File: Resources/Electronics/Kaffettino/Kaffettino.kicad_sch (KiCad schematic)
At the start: 6 parts, among them SW1 SW_Push, SW2 SW_Push, SW3 SW_Push

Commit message: PCB Design - continuing schema
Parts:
- removed SW1, SW2, SW3: SW_Push, symbol Switch:SW_Push
- added Brd1: SSD1306, Display:Adafruit_SSD1306, symbol SSD1306-128x64_OLED:SSD1306
- added C1, C2, C3: 100nF, symbol Device:C
- added J1: 1984659, CONN_1984659_PXC, symbol 2025-11-03_20-57-13:1984659
- added M1: RFID-RC522, RFID-RC522:RFID-RC522, symbol RFID-RC522:RFID-RC522
- added R1, R2, R3: 330, symbol Device:R
- added R4, R5, R6: 1k, symbol Device:R
- added R7, R8, R9: 10k, symbol Device:R
- D1: value LED -> Green
- D2: value LED -> Yellow
- D3: value LED -> Red
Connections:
- net at D3.1 (K): now also R3.1
- net at D2.1 (K): now also R2.1
- net at D1.1 (K): now also R1.1
- new net: C1.1, R4.1, R7.2
- new net: J1.4, R4.2
- new net: C2.1, R6.1, R9.2
- new net: C3.1, R5.1, R8.2
- new net: J1.5, R6.2
- new net: J1.6, R5.2
- new net +3.3V: R7.1, R8.1, R9.1
- new net GNDREF: Brd1.1 (GND), C1.2, C2.2, C3.2, J1.1, J1.2, J1.3, M1.6 (GND), R1.2, R2.2, R3.2
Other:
- company: (none) -> Vivere Ingegneria
- title: (none) -> Scheda superiore kaffettino
- moved on the sheet: D1, D2, D3

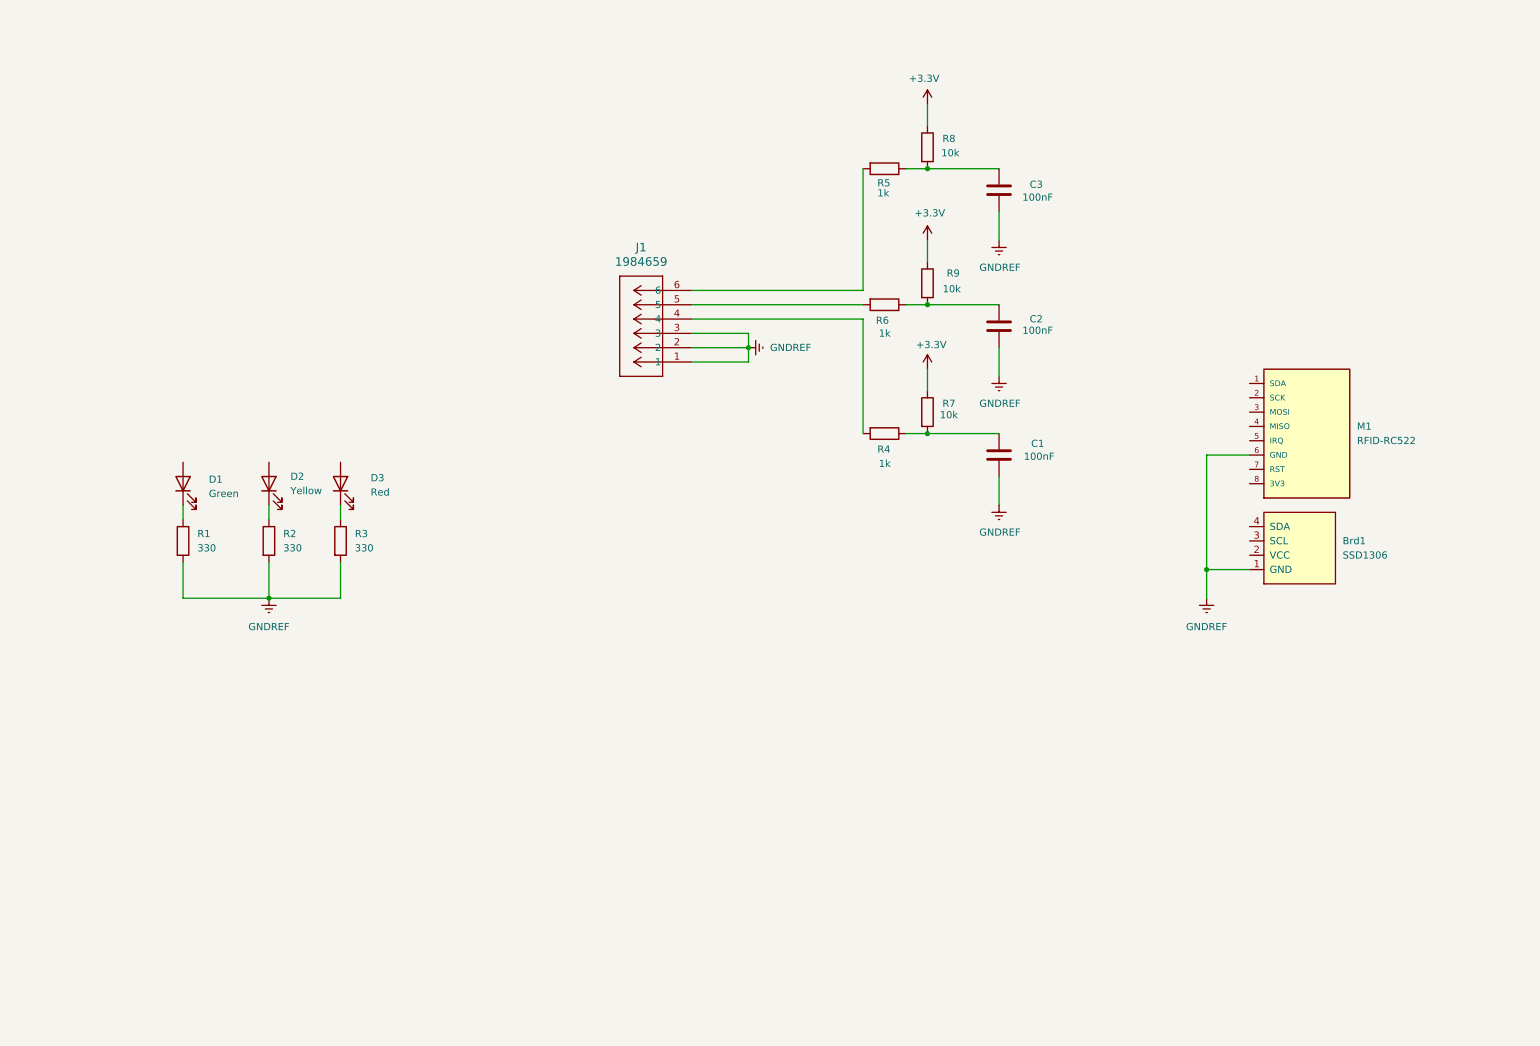
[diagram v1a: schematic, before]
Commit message: Finished electrical schema and removed node_modules
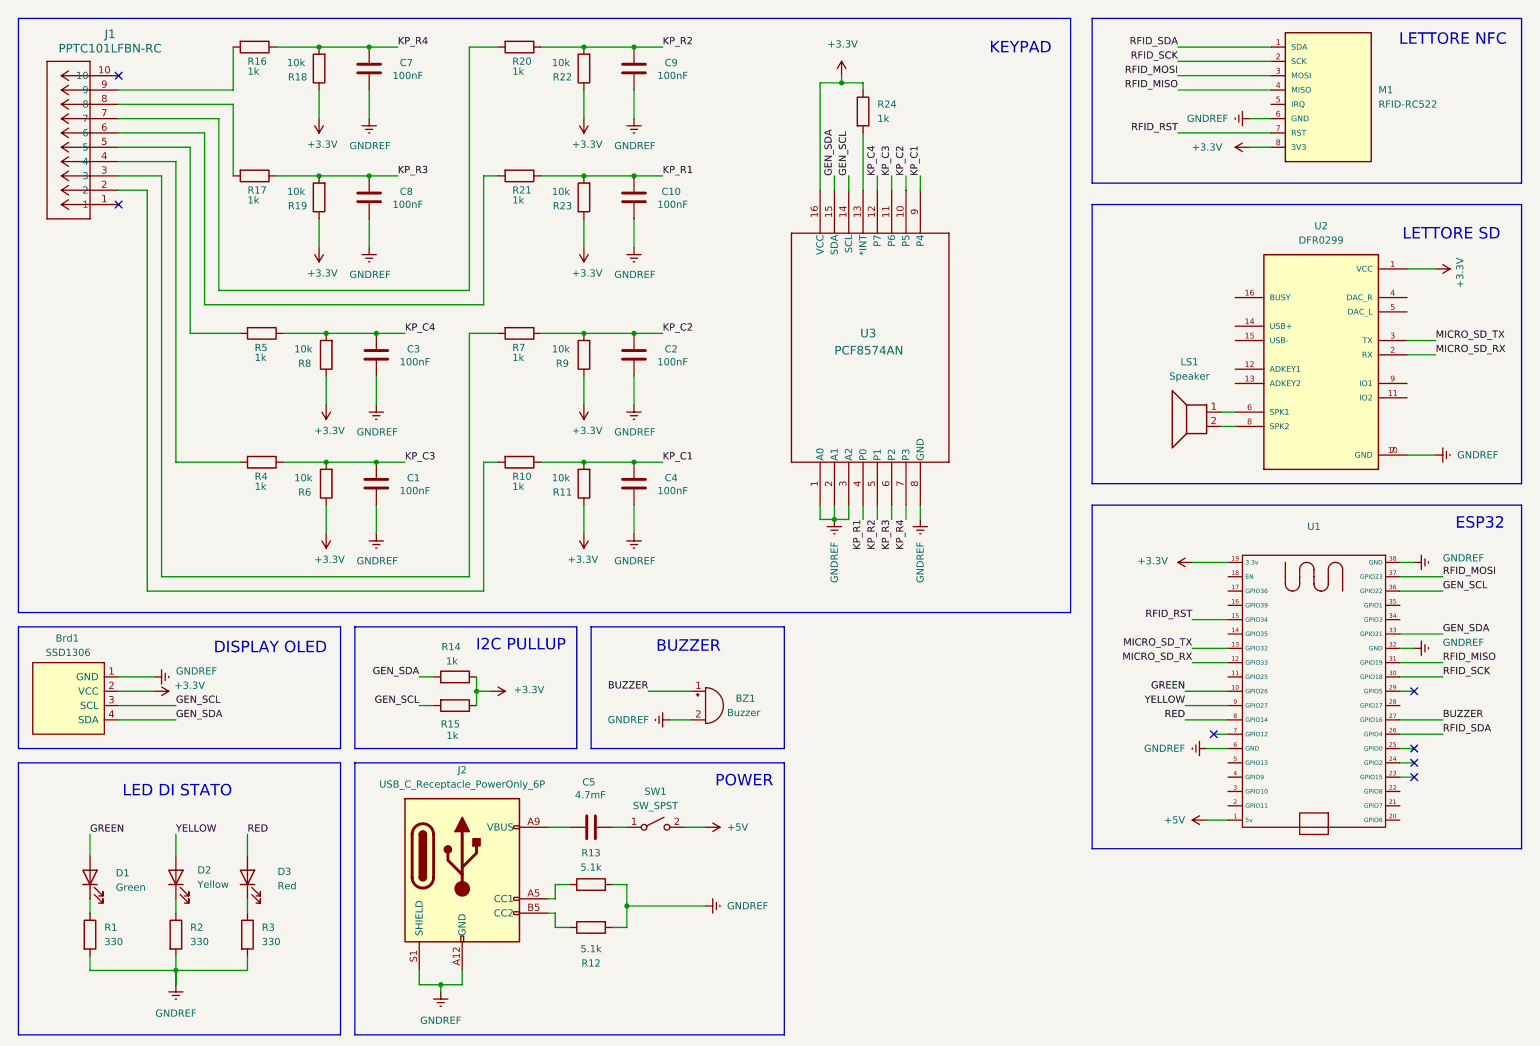
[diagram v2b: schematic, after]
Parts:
- removed J1: 1984659, CONN_1984659_PXC, symbol 2025-11-03_20-57-13:1984659
- added BZ1: Buzzer, Buzzer_Beeper:Buzzer_12x9.5RM7.6, symbol Device:Buzzer
- added C10, C4, C7, C8, C9: 100nF, Capacitor_THT:C_Disc_D3.0mm_W1.6mm_P2.50mm, symbol Device:C
- added C5: 4.7mF, Capacitor_THT:C_Disc_D3.0mm_W1.6mm_P2.50mm, symbol Device:C
- added J1: PPTC101LFBN-RC, PPTC101LFBN_RC:CONN10_101LFBN-RC_SUL, symbol PPTC101LFBN_RC:PPTC101LFBN-RC
- added J2: USB_C_Receptacle_PowerOnly_6P, Connector_USB:USB_C_Receptacle_GCT_USB4125-xx-x_6P_TopMnt_Horizontal, symbol Connector:USB_C_Receptacle_PowerOnly_6P
- added LS1: Speaker, OSTVN02A150:CONN_OSTVN02A150_OST, symbol Device:Speaker
- added R10, R14, R15, R16, R17, R20, R21, R24: 1k, Resistor_THT:R_Axial_DIN0207_L6.3mm_D2.5mm_P10.16mm_Horizontal, symbol Device:R
- added R11, R18, R19, R22, R23: 10k, Resistor_THT:R_Axial_DIN0207_L6.3mm_D2.5mm_P10.16mm_Horizontal, symbol Device:R
- added R12, R13: 5.1k, Resistor_THT:R_Axial_DIN0207_L6.3mm_D2.5mm_P10.16mm_Horizontal, symbol Device:R
- added SW1: SW_SPST, symbol Switch:SW_SPST
- added U1: ~, ESP32-38Pin:ESP32_38pin, symbol esp32_38pin:ESP32_38Pin
- added U2: DFR0299, DFR0299:MODULE_DFR0299, symbol DFR0299:DFR0299
- added U3: PCF8574AN, PCF8574AN:N16, symbol 2025-11-11_17-54-51:PCF8574AN
- C1, C2, C3: footprint (none) -> Capacitor_THT:C_Disc_D3.0mm_W1.6mm_P2.50mm
- R1, R2, R3, R4, R5, R8, R9: footprint (none) -> Resistor_THT:R_Axial_DIN0207_L6.3mm_D2.5mm_P10.16mm_Horizontal
- R6: value 1k -> 10k; footprint (none) -> Resistor_THT:R_Axial_DIN0207_L6.3mm_D2.5mm_P10.16mm_Horizontal
- R7: value 10k -> 1k; footprint (none) -> Resistor_THT:R_Axial_DIN0207_L6.3mm_D2.5mm_P10.16mm_Horizontal
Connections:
- net +3.3V: now also Brd1.2 (VCC), M1.8 (3V3), R6.1, R11.1, R14.1, R15.1, R18.1, R19.1, R22.1, R23.1, R24.1, U1.19 (3.3v), U2.1 (VCC), U3.16 (VCC); no longer R7.1
- net GNDREF: now also BZ1.2 (-), C10.2, C4.2, C7.2, C8.2, C9.2, J2.A12 (GND), J2.B12 (GND), J2.S1 (SHIELD), R12.2, R13.2, U1.32 (GND), U1.38 (GND), U1.6 (GND), U2.10 (GND), U2.7 (GND), U3.1 (A0), U3.2 (A1), U3.3 (A2), U3.8 (GND)
- net RED: now reaches D3.2 (A)
- net RED: now also U1.8 (GPIO14)
- net KP_C3: now reaches C1.1, R4.1
- net KP_C3: now also R6.2, U3.11 (P6); no longer R7.2
- net at R4.2: now also J1.4
- net KP_C2: now reaches C2.1, R9.2
- net KP_C2: now also R7.1, U3.10 (P5); no longer R6.1
- net KP_C4: now reaches C3.1, R5.1, R8.2
- net KP_C4: now also U3.12 (P7)
- net at R5.2: now also J1.5
- net YELLOW: now reaches D2.2 (A)
- net YELLOW: now also U1.9 (GPIO27)
- net RFID_SDA: now reaches M1.1 (SDA)
- net RFID_SDA: now also U1.26 (GPIO4)
- net RFID_SCK: now reaches M1.2 (SCK)
- net RFID_SCK: now also U1.30 (GPIO18)
- net RFID_MOSI: now reaches M1.3 (MOSI)
- net RFID_MOSI: now also U1.37 (GPIO23)
- net RFID_MISO: now reaches M1.4 (MISO)
- net RFID_MISO: now also U1.31 (GPIO19)
- net RFID_RST: now reaches M1.7 (RST)
- net RFID_RST: now also U1.15 (GPIO34)
- net GREEN: now reaches D1.2 (A)
- net GREEN: now also U1.10 (GPIO26)
- net GEN_SCL: now reaches Brd1.3 (SCL)
- net GEN_SCL: now also R15.2, U1.36 (GPIO22), U3.14 (SCL)
- net GEN_SDA: now reaches Brd1.4 (SDA)
- net GEN_SDA: now also R14.2, U1.33 (GPIO21), U3.15 (SDA)
- new net: R24.2, U3.13 (*INT)
- new net: J1.7, R20.2
- new net: J2.A5 (CC1), R13.1
- new net: C5.1, J2.A9 (VBUS), J2.B9 (VBUS)
- new net: J2.B5 (CC2), R12.1
- new net: C5.2, SW1.1 (A)
- new net: LS1.1, U2.6 (SPK1)
- new net: LS1.2, U2.8 (SPK2)
- new net: J1.8, R17.2
- new net: J1.3, R7.2
- new net: J1.6, R21.2
- new net: J1.2, R10.2
- new net: J1.9, R16.2
- new net +5V: SW1.2 (B), U1.1 (5v)
- new net BUZZER: BZ1.1 (+), U1.27 (GPIO16)
- new net KP_C1: C4.1, R10.1, R11.2, U3.9 (P4)
- new net KP_R1: C10.1, R21.1, R23.2, U3.4 (P0)
- new net KP_R2: C9.1, R20.1, R22.2, U3.5 (P1)
- new net KP_R3: C8.1, R17.1, R19.2, U3.6 (P2)
- new net KP_R4: C7.1, R16.1, R18.2, U3.7 (P3)
- new net MICRO_SD_RX: U1.12 (GPIO33), U2.2 (RX)
- new net MICRO_SD_TX: U1.13 (GPIO32), U2.3 (TX)
- no-connect marks 0 -> 7
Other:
- note added: "BUZZER"
- note added: "DISPLAY OLED"
- note added: "ESP32"
- note added: "I2C PULLUP"
- note added: "KEYPAD"
- note added: "LED DI STATO"
- note added: "LETTORE NFC"
- note added: "LETTORE SD"
- note added: "POWER"
- title: Scheda superiore kaffettino -> PCB Kaffettino
- moved on the sheet: Brd1, C3, D1, D2, D3, M1, R1, R2, R3, R5, R8

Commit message: Added expansion pins and changed power method in electrical schema
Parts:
- removed J2: USB_C_Receptacle_PowerOnly_6P, Connector_USB:USB_C_Receptacle_GCT_USB4125-xx-x_6P_TopMnt_Horizontal, symbol Connector:USB_C_Receptacle_PowerOnly_6P
- removed R13: 5.1k, Resistor_THT:R_Axial_DIN0207_L6.3mm_D2.5mm_P10.16mm_Horizontal, symbol Device:R
- removed SW1: SW_SPST, symbol Switch:SW_SPST
- added J2, J3, J4, J5: OSTVN02A150, OSTVN02A150:CONN_OSTVN02A150_OST, symbol 2025-11-11_16-38-17:OSTVN02A150
- added R23: 1k, Resistor_THT:R_Axial_DIN0207_L6.3mm_D2.5mm_P10.16mm_Horizontal, symbol Device:R
- C10: renamed from C5; value 4.7mF -> 4.7uF; footprint Capacitor_THT:C_Disc_D3.0mm_W1.6mm_P2.50mm -> Capacitor_THT:CP_Radial_D6.3mm_P2.50mm
- R12: value 5.1k -> 1k
- R25: renamed from R24; value 1k -> 10k
- U2: renamed from U1; value ~ -> ESP32-38Pin-Wroom
- renumbered C7 to C1, C8 to C2, C1 to C4, C9 to C6, C10 to C7, C2 to C8, C4 to C9, R8 to R10, R6 to R11, R14 to R13, R15 to R14, R20 to R15, R21 to R16, R7 to R17, R10 to R18, R22 to R19, R23 to R20, R9 to R21, R11 to R22, R16 to R4, R17 to R5, R5 to R6, R4 to R7, R18 to R8, R19 to R9, U3 to U1, U2 to U3
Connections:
- net +5V: now also C10.1, J2.1
- net GEN_SCL: now also J5.1
- net GEN_SDA: now also J5.2
- net GNDREF: now also C10.2, J2.2, J3.2, J4.2; no longer R12.2
- net GREEN: now also U2.11 (GPIO25); no longer U2.10 (GPIO26)
- net MICRO_SD_RX: now also R23.1; no longer U3.2 (RX)
- net MICRO_SD_TX: now also R12.1; no longer U3.3 (TX)
- net RED: now also U2.9 (GPIO27); no longer U2.8 (GPIO14)
- net YELLOW: now also U2.10 (GPIO26); no longer U2.9 (GPIO27)
- net KP_INT: now reaches R25.2, U1.13 (*INT)
- net KP_INT: now also U2.17 (GPIO36)
- net RFID_INT: now reaches M1.5 (IRQ)
- net RFID_INT: now also U2.16 (GPIO39)
- net EXPANSION_1: now reaches U2.14 (GPIO35)
- net EXPANSION_1: now also J3.1
- net EXPANSION_2: now reaches U2.28 (GPIO17)
- net EXPANSION_2: now also J4.1
- new net: R23.2, U3.2 (RX)
- new net: R12.2, U3.3 (TX)
- no-connect marks 7 -> 27
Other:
- note added: "EXPANSION PIN I2C"
- note added: "EXPANSION PINS"
- moved on the sheet: BZ1, C10, LS1, R10, R13, R14, R25, U2, U3
